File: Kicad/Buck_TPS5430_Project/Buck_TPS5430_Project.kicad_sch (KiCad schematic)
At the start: 26 parts

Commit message: WIP: add capacitor and powergood led
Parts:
- added C? (x2): 47u, symbol Device:C
- added C?: 0.1u, symbol Device:C
- added C?: 10u, symbol Device:C
- added C?: 220uF, symbol Device:C_Polarized_US
- added D?: LED, symbol Device:LED
- added R? (x5): ~, symbol Device:R_US
- added U? (x3): LM393, symbol Comparator:LM393
- added U?: TL431DBZ, Package_TO_SOT_SMD:SOT-23, symbol Reference_Voltage:TL431DBZ
- C?: value C -> 10u
- C?: value C -> 0.01u
- L?: value L -> 15u
- TP?: value TestPoint -> TP_VIN
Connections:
- net GND: now also U?.1 (GND), C?.2, C?.2, C?.2, C?.2, C?.2, R?.1, U?.3 (A), U?.4 (V-)
- net OUT-: no longer U?.1 (GND)
- net VSENSE: now reaches J?.1 (Pin_1), J?.1 (Pin_1), J?.1 (Pin_1), R?.2, U?.4 (VSENSE)
- net VSENSE: now also U?.2 (-)
- net at C?.1, U?.7 (VIN): now also C?.1, C?.1, C?.1
- net at C?.1, L?.2, R?.1: now also C?.1, C?.1
- net VCC renamed VIN
- net VIN: now also R?.1, U?.8 (V+)
- new net: D?.1 (K), R?.2, U?.1
- new net: R?.1, R?.1, R?.2, U?.3 (+)
- new net: D?.2 (A), R?.1
- new net: R?.2, R?.2, R?.2, U?.1 (K), U?.2 (REF)
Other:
- moved on the sheet: C?, D?, J?, L?, R?, SW?, U?

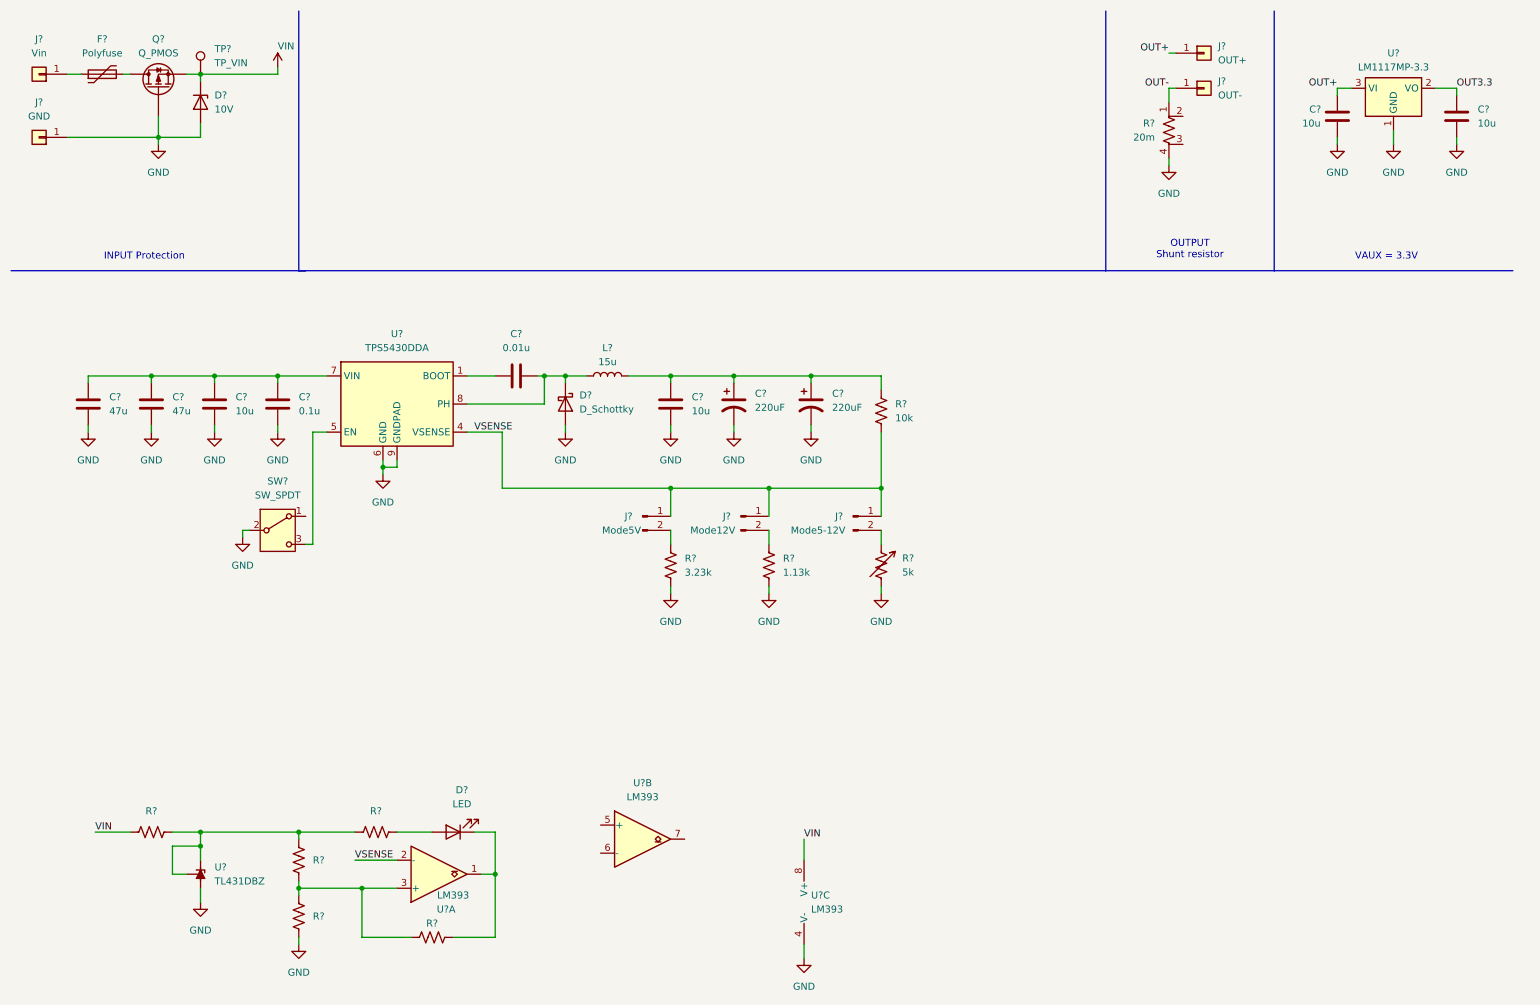
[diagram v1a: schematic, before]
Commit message: WIP: compelete powergood led and add short current protection
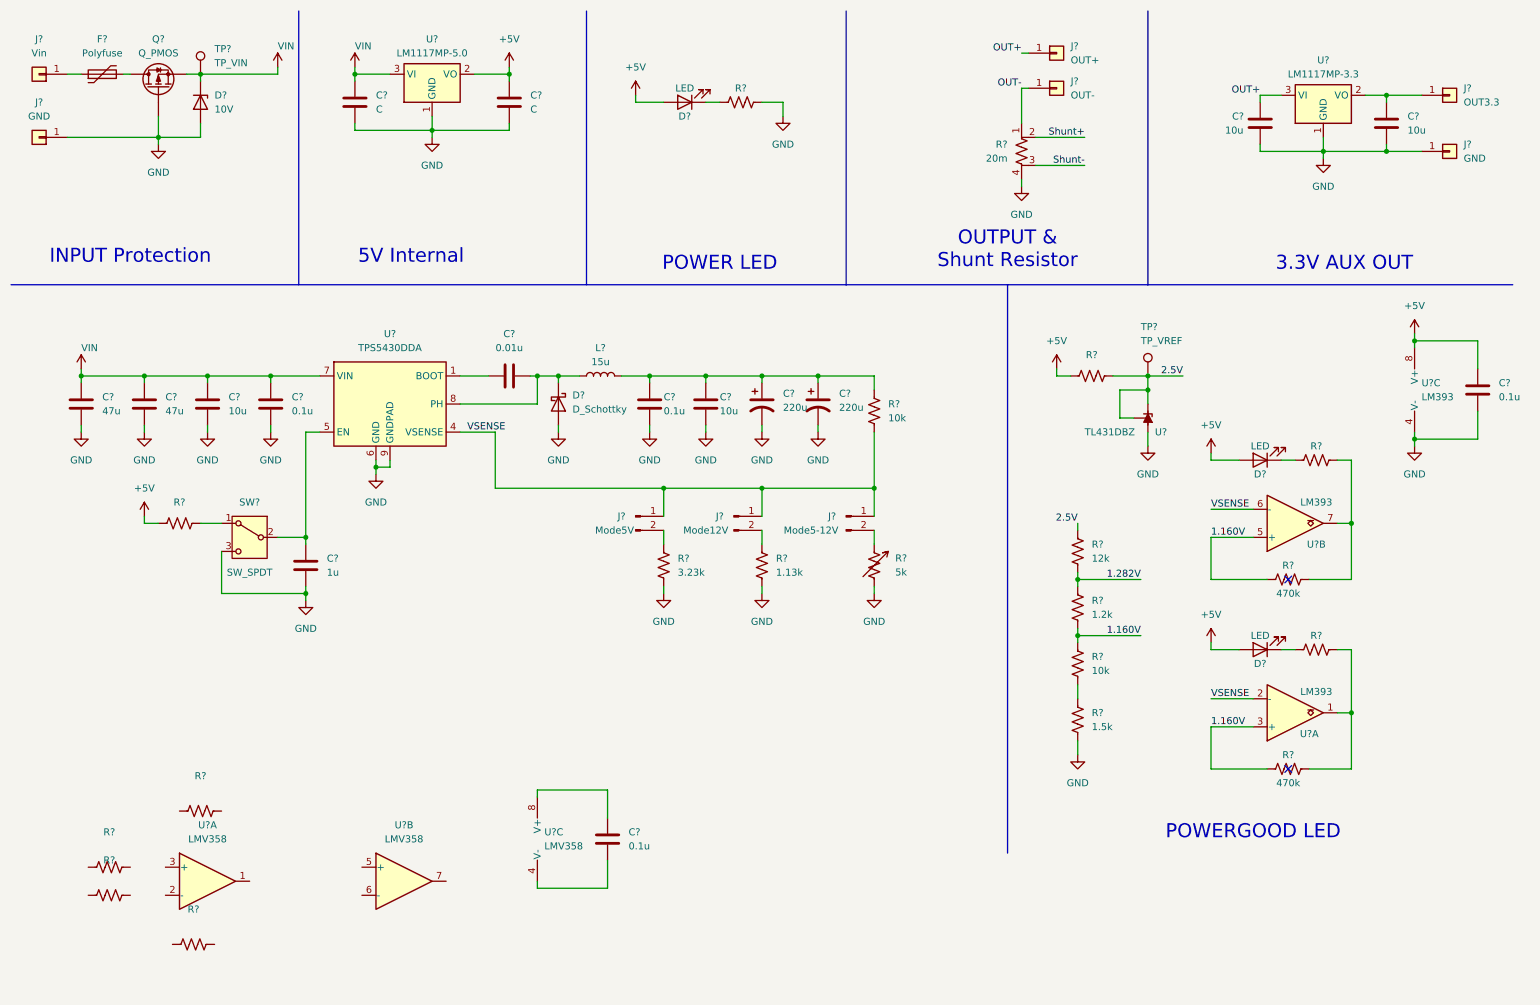
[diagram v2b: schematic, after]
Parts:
- removed D?: LED, symbol Device:LED
- removed R? (x4): ~, symbol Device:R_US
- removed SW?: SW_SPDT, symbol Switch:SW_SPDT
- removed U?: TL431DBZ, Package_TO_SOT_SMD:SOT-23, symbol Reference_Voltage:TL431DBZ
- removed U?: LM393, symbol Comparator:LM393
- added C? (x2): 0.1u, symbol Device:C
- added C? (x2): C, symbol Device:C
- added C?: 1u, symbol Device:C
- added C?: 10u, symbol Device:C
- added D? (x3): LED, symbol Device:LED
- added J?: OUT3.3, symbol Connector_Generic:Conn_01x01
- added J?: GND, symbol Connector_Generic:Conn_01x01
- added R? (x9): ~, symbol Device:R_US
- added R?: 470k, symbol Device:R_US
- added R?: 1.2k, symbol Device:R_US
- added R?: 1.5k, symbol Device:R_US
- added R?: 12k, symbol Device:R_US
- added R?: 10k, symbol Device:R_US
- added SW?: SW_SPDT, symbol Switch:SW_SPDT
- added TP?: TP_VREF, symbol Connector:TestPoint
- added U? (x3): LMV358, symbol Amplifier_Operational:LMV358
- added U?: TL431DBZ, Package_TO_SOT_SMD:SOT-23, symbol Reference_Voltage:TL431DBZ
- added U?: LM1117MP-5.0, Package_TO_SOT_SMD:SOT-223-3_TabPin2, symbol Regulator_Linear:LM1117MP-5.0
- added U?: LM393, symbol Comparator:LM393
- C? (x2): value 220uF -> 220u
- C?: value 10u -> 0.1u
- R?: value ~ -> 470k
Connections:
- net GND: now also C?.2, C?.2, C?.2, C?.2, C?.2, J?.1 (Pin_1), R?.1, R?.1, SW?.3 (C), U?.1 (GND), U?.3 (A)
- net VIN: now also C?.1, C?.1, C?.1, C?.1, U?.7 (VIN), C?.1, U?.3 (VI); no longer U?.8 (V+)
- net VSENSE: now also U?.6 (-)
- net at U?.5 (EN): now also C?.1, SW?.2 (B)
- net Shunt+: now reaches R?.2
- net Shunt-: now reaches R?.3
- net at R?.2, U?.1: now also R?.1
- net 1.160V: now reaches R?.1, U?.3 (+)
- net 1.160V: now also R?.1, R?.1, R?.2, U?.5 (+)
- net at C?.1, C?.1, C?.1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: now also C?.1
- net OUT3.3: no longer names the net of C?.2, U?.2 (VO)
- net OUT3.3: now also J?.1 (Pin_1)
- new net: R?.1, R?.2, U?.7
- new net: C?.1, U?.8 (V+)
- new net: C?.2, U?.4 (V-)
- new net: D?.1 (K), R?.2 (x3)
- new net: R?.1, R?.2
- new net: R?.2, SW?.1 (A)
- new net +5V: C?.1, C?.1, D?.2 (A), D?.2 (A), D?.2 (A), R?.1, R?.1, U?.2 (VO), U?.8 (V+)
- new net 1.282V: R?.1, R?.2
- new net 2.5V: R?.2, R?.2, TP?.1, U?.1 (K), U?.2 (REF)
- no-connect marks 0 -> 2
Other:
- note added: "3.3V AUX OUT"
- note added: "5V Internal"
- note added: "OUTPUT & Shunt Resistor"
- note added: "POWER LED"
- note added: "POWERGOOD LED"
- note removed: "OUTPUT Shunt resistor"
- note removed: "VAUX = 3.3V"
- moved on the sheet: C?, D?, J?, L?, R?, U?, U?A, U?C

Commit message: feat: finish schematic topology (values TBD - to be determined)
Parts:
- removed D?: LED, symbol Device:LED
- removed R?: ~, symbol Device:R_US
- removed TP?: TP_VIN, symbol Connector:TestPoint
- removed U? (x3): LM393, symbol Comparator:LM393
- added C?: 10n, symbol Device:C
- added C?: 0.01u, symbol Device:C
- added C?: 1u, symbol Device:C
- added D?: D_Schottky, symbol Device:D_Schottky
- added D?: LED, symbol Device:LED
- added R?: 470k, symbol Device:R_US
- added R? (x4): ~, symbol Device:R_US
- added R?: 100, symbol Device:R_US
- added R?: 1k, symbol Device:R_US
- added R?: 5k, symbol Device:R_Variable_US
- added TP?: TP_VIN, symbol Connector:TestPoint
- added TP?: TP_PH, symbol Connector:TestPoint
- added TP?: TP_VSHUNT, symbol Connector:TestPoint
- added TP?: TP_VP, symbol Connector:TestPoint
- added TP? (x2): TP_GNDVP, symbol Connector:TestPoint
- added TP?: TP_1.160V, symbol Connector:TestPoint
- added TP?: TP_GNDVIN, symbol Connector:TestPoint
- added TP?: TP_5V, symbol Connector:TestPoint
- added TP?: TP_EN, symbol Connector:TestPoint
- added TP?: TP_FB, symbol Connector:TestPoint
- added TP?: TP_AUX, symbol Connector:TestPoint
- added TP?: TP_1.282V, symbol Connector:TestPoint
- added U? (x5): LM339, symbol Comparator:LM339
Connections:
- net +5V: now also C?.1, U?.8 (V+), C?.1, D?.2 (A), R?.2, TP?.1, U?.3 (V+)
- net 1.160V: now also TP?.1, U?.7 (+); no longer R?.1
- net 1.282V: now also R?.1, TP?.1, U?.5 (+)
- net GND: now also C?.2, R?.2, U?.4 (V-), C?.2, C?.2, R?.1, R?.2, R?.2, TP?.1, TP?.1, U?.12 (V-); no longer D?.2 (A), Q?.G, R?.2
- net OUT+: now also TP?.1
- net OUT-: now also TP?.1
- net Shunt+: now also R?.1
- net Shunt-: now also R?.1
- net VIN: now also TP?.1
- net VSENSE: now also R?.1, TP?.1
- net at R?.2: now also R?.1, U?.2
- net at R?.2: now also R?.1, U?.2 (-)
- net at C?.2, D?.1 (K), L?.1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: now also TP?.1
- net at R?.1, R?.2: now also U?.1
- net ENA: now reaches C?.1, SW?.2 (B), U?.5 (EN)
- net ENA: now also D?.1 (K), TP?.1, U?.13
- net at C?.2, J?.1 (Pin_1), U?.2 (VO): now also TP?.1
- net at R?.1: now also R?.2, U?.3 (+)
- net at R?.2: now also U?.1, R?.1
- new net: D?.2 (A), R?.1
- new net: D?.2 (A), Q?.G, R?.1
- new net: R?.2, U?.4 (-), U?.6 (-)
- new net: C?.1, C?.2, R?.1, R?.1, R?.2, U?.11 (+)
- new net: C?.1, R?.2, TP?.1, U?.10 (-)
- new net: D?.1 (K), R?.2
- new net: R?.2, R?.2
- no-connect marks 2 -> 8
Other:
- note added: "Control Power Supply"
- note added: "Overcurrent Protection"
- moved on the sheet: C?, D?, J?, L?, R?, SW?, TP?, U?, U?A, U?B, U?C

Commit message: feat: add 5v buck, edit logic of power led, calculate R, L, C
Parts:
- removed C? (x2): 47u, symbol Device:C
- removed C? (x2): 10u, symbol Device:C
- removed C?: 0.1u, symbol Device:C
- removed C?: 220u, symbol Device:C_Polarized_US
- removed D?: LED, symbol Device:LED
- removed J?: Mode5V, symbol Connector:Conn_01x02_Pin
- removed J?: Mode12V, symbol Connector:Conn_01x02_Pin
- removed J?: Mode5-12V, symbol Connector:Conn_01x02_Pin
- removed R? (x3): 470k, symbol Device:R_US
- removed R?: 1k, symbol Device:R_US
- removed R?: 3.23k, symbol Device:R_US
- removed R?: 1.2k, symbol Device:R_US
- removed R?: 1.5k, symbol Device:R_US
- removed R?: 12k, symbol Device:R_US
- removed R?: 1.13k, symbol Device:R_US
- removed R?: 10k, symbol Device:R_US
- removed R?: 5k, symbol Device:R_Variable_US
- removed R?: ~, symbol Device:R_US
- removed SW?: SW_SPDT, symbol Switch:SW_SPDT
- removed TP?: TP_1.160V, symbol Connector:TestPoint
- removed TP?: TP_1.282V, symbol Connector:TestPoint
- removed U?: LM1117MP-3.3, Package_TO_SOT_SMD:SOT-223-3_TabPin2, symbol Regulator_Linear:LM1117MP-3.3
- added C1, C2, C20, C21, C23, C25, C26, C3, C4: 47u, symbol Device:C_Polarized_US
- added C12, C15, C18, C31: 0.1u, symbol Device:C
- added C16: 10n, symbol Device:C
- added C5, C6, C7, C8: 4.7u, symbol Device:C_Polarized_US
- added D4: D_Schottky, symbol Device:D_Schottky
- added D6, D7, D9: LED, symbol Device:LED
- added J3: Mode5V, symbol Connector:Conn_01x02_Pin
- added J4: Mode12V, symbol Connector:Conn_01x02_Pin
- added J5: Mode3.3-12V, symbol Connector:Conn_01x02_Pin
- added L2: 30-50u, symbol Device:L
- added R11, R12: ~, symbol Device:R_US
- added R13: 1.13k, symbol Device:R_US
- added R16, R23: 10k, symbol Device:R_US
- added R17: 5k 10%, symbol Device:R_Variable_US
- added R18: 1k 1%, symbol Device:R_US
- added R21: 12k, symbol Device:R_US
- added R22: 1.2k, symbol Device:R_US
- added R25: 1.5k, symbol Device:R_US
- added R9: 3.23k, symbol Device:R_US
- added TP11: TP_FB2, symbol Connector:TestPoint
- added TP13: TP_PH2, symbol Connector:TestPoint
- added TP16: TP_7.3V, symbol Connector:TestPoint
- added TP20: TP_1.282V, symbol Connector:TestPoint
- added TP21: TP_1.160V, symbol Connector:TestPoint
- added TP3: TP_VIN2, symbol Connector:TestPoint
- added TP4: TP_GNDVIN2, symbol Connector:TestPoint
- added TP6: TP_EN2, symbol Connector:TestPoint
- added TP9: TP_GND, symbol Connector:TestPoint
- added U3: TPS5430DDA, Package_SO:TI_SO-PowerPAD-8_ThermalVias, symbol Regulator_Switching:TPS5430DDA
- added U6: LD1117S33TR_SOT223, Package_TO_SOT_SMD:SOT-223-3_TabPin2, symbol Regulator_Linear:LD1117S33TR_SOT223
- C10: renamed from C?; value 0.01u -> 10n
- C11: renamed from C?; value 1u -> 0.1u
- C14: renamed from C?; value 0.01u -> 0.1u
- C22: renamed from C?; value 220u -> 47u
- C27: renamed from C?; value C -> 0.33u
- C28: renamed from C?; value 10u -> 0.1u
- C29: renamed from C?; value C -> 0.1u
- D1: renamed from D?; value 10V -> ZMM10 10V
- F1: renamed from F?; value Polyfuse -> UF300
- L1: renamed from L?; value 15u -> 20-25u
- Q1: renamed from Q?; value Q_PMOS -> APM4015P
- R1: renamed from R?; value ~ -> 4.7k 5%
- R15: renamed from R?; value ~ -> 2k 1%
- R2, R3: renamed from R?; value ~ -> 1k 1%
- R4, R5: renamed from R?; value ~ -> 50k 1%
- R6: renamed from R?; value ~ -> 10k
- R7: renamed from R?; value 5k -> 100k
- TP1: renamed from TP?; value TP_VIN -> TP_VIN1
- TP10: renamed from TP?; value TP_FB -> TP_FB1
- TP12: renamed from TP?; value TP_PH -> TP_PH1
- TP2: renamed from TP?; value TP_GNDVIN -> TP_GNDVIN1
- TP5: renamed from TP?; value TP_EN -> TP_EN1
- TP8: renamed from TP?; value TP_GNDVP -> TP_GND
- U5: renamed from U?; value LM1117MP-5.0 -> LM7805R 5V 1.5A
- gave numbers to parts that had none: 33
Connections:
- net +5V: now also C28.2, R26.2, D6.2 (A), D7.2 (A), U6.3 (VI)
- net 1.160V: now also R22.2, R23.1, TP21.1
- net 1.282V: now also R21.2, R22.1, TP20.1
- net ENA: now also C16.1; no longer C11.1, TP5.1, U2.5 (EN)
- net GND: now also C1.2, C12.2, C16.2, C18.2, C2.2, C20.2, C21.2, C23.2, C25.2, C26.2, C3.2, C31.1, C4.2, C5.2, C6.2, C7.2, C8.2, D4.2 (A), D9.1 (K), R13.2, R18.1, R25.2, R9.2, TP4.1, TP9.1, U3.6 (GND), U3.9 (GNDPAD), U6.1 (GND)
- net OUT+: now also C18.1, C21.1, C23.1, C26.1, L2.2, R16.1; no longer C28.2
- net VIN: now also C1.1, C2.1, C3.1, C4.1, C5.1, C6.1, C7.1, C8.1, TP3.1, U3.7 (VIN); no longer C27.1, U5.3 (VI)
- net VSENSE: now also R15.2, U1.5 (+), J3.1 (Pin_1), J4.1 (Pin_1), J5.1 (Pin_1), R16.2, TP11.1, U3.4 (VSENSE)
- net at R26.1, U4.2: now also D9.2 (A)
- net at U4.4 (-), U4.6 (-): now also U1.6 (-), U1.7, C31.2
- net at C13.1, TP7.1, U4.10 (-): now also R5.2, U1.1
- net at C30.2, J8.1 (Pin_1), TP18.1: now also U6.2 (VO)
- net 7.326V: now reaches C17.1, C22.1, L1.2, R14.1
- net 7.326V: now also C27.1, U5.3 (VI), C20.1, C25.1, TP16.1
- net 2.5V: no longer names the net of R20.2, TP19.1, U7.1 (K), U7.2 (REF)
- net 2.5V: now also R21.1
- new net: D6.1 (K), R11.2
- new net: C15.1, U3.1 (BOOT)
- new net: C15.2, D4.1 (K), L2.1, TP13.1, U3.8 (PH)
- new net: R23.2, R25.1
- new net: R17.2, R18.2
- new net: D7.1 (K), R12.2
- new net: J3.2 (Pin_2), R9.1
- new net: J4.2 (Pin_2), R13.1
- new net: J5.2 (Pin_2), R17.1
- new net ENA1: C11.1, R11.1, TP5.1, U2.5 (EN)
- new net ENA2: C12.1, R12.1, TP6.1, U3.5 (EN)
- no-connect marks 8 -> 3
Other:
- note added: "TPS5430 Buck Regulator"
- moved on the sheet: C10, C11, C13, C14, C19, C24, C27, C29, C9, D2, D5, D8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
